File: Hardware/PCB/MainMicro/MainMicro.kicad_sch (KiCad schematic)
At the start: 56 parts, among them J1 Conn_02x05_Odd_Even, J10 Conn_01x03_Male, J11 Conn_01x05_Male, J12 Conn_01x05_Male, J2 USB_B_Mini, J3 Barrel_Jack, J4 Conn_01x05_Male, J5 Conn_01x06_Male, J6 Conn_01x06_Male, J7 Conn_01x03_Male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

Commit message: PCB passing DRC
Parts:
- added R16, R17, R18, R19, R20, R21: 10, Resistor_SMD:R_0805_2012Metric_Pad1.20x1.40mm_HandSolder, symbol Device:R
- J2: footprint Connector_USB:USB_Micro-AB_Molex_47590-0001 -> Connector_USB:USB_Micro-B_Amphenol_10118194_Horizontal
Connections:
- net DIR1+: now also R17.2; no longer U5.20 (B2)
- net DIR2+: now also R20.2; no longer U5.17 (B5)
- net EN1+: now also R18.2; no longer U5.19 (B3)
- net EN2+: now also R21.2; no longer U5.16 (B6)
- net PUL1+: now also R16.2; no longer U5.21 (B1)
- net PUL2+: now also R19.2; no longer U5.18 (B4)
- new net: R21.1, U5.16 (B6)
- new net: R19.1, U5.18 (B4)
- new net: R17.1, U5.20 (B2)
- new net: R16.1, U5.21 (B1)
- new net: R20.1, U5.17 (B5)
- new net: R18.1, U5.19 (B3)
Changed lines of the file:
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@@
     (stroke (width 0) (type default) (color 0 0 0 0))
   )
-  (wire (pts (xy 350.52 128.27) (xy 381 128.27))
+  (wire (pts (xy 350.52 128.27) (xy 360.68 128.27))
     (stroke (width 0) (type default) (color 0 0 0 0))
   )
@@
     (stroke (width 0) (type default) (color 0 0 0 0))
   )
+  (wire (pts (xy 368.3 135.89) (xy 381 135.89))
+    (stroke (width 0) (type default) (color 0 0 0 0))
+  )
   (wire (pts (xy 179.07 88.9) (xy 179.07 93.98))
     (stroke (width 0) (type default) (color 0 0 0 0))
@@
     (stroke (width 0) (type default) (color 0 0 0 0))
   )
+  (wire (pts (xy 368.3 118.11) (xy 381 118.11))
+    (stroke (width 0) (type default) (color 0 0 0 0))
+  )
   (wire (pts (xy 181.61 190.5) (xy 179.07 190.5))
     (stroke (width 0) (type default) (color 0 0 0 0))
@@
     (stroke (width 0) (type default) (color 0 0 0 0))
   )
-  (wire (pts (xy 355.6 118.11) (xy 381 118.11))
+  (wire (pts (xy 355.6 118.11) (xy 360.68 118.11))
     (stroke (width 0) (type default) (color 0 0 0 0))
   )
@@
     (stroke (width 0) (type default) (color 0 0 0 0))
   )
+  (wire (pts (xy 368.3 140.97) (xy 381 140.97))
+    (stroke (width 0) (type default) (color 0 0 0 0))
+  )
   (wire (pts (xy 356.87 198.12) (xy 363.22 198.12))
     (stroke (width 0) (type default) (color 0 0 0 0))
@@
     (stroke (width 0) (type default) (color 0 0 0 0))
   )
+  (wire (pts (xy 368.3 128.27) (xy 381 128.27))
+    (stroke (width 0) (type default) (color 0 0 0 0))
+  )
   (wire (pts (xy 34.29 217.17) (xy 49.53 217.17))
     (stroke (width 0) (type default) (color 0 0 0 0))
@@
     (stroke (width 0) (type default) (color 0 0 0 0))
   )
-  (wire (pts (xy 358.14 135.89) (xy 381 135.89))
+  (wire (pts (xy 358.14 135.89) (xy 360.68 135.89))
     (stroke (width 0) (type default) (color 0 0 0 0))
   )
@@
     (stroke (width 0) (type default) (color 0 0 0 0))
   )
-  (wire (pts (xy 358.14 123.19) (xy 381 123.19))
+  (wire (pts (xy 358.14 123.19) (xy 360.68 123.19))
     (stroke (width 0) (type default) (color 0 0 0 0))
   )
@@
     (stroke (width 0) (type default) (color 0 0 0 0))
   )
-  (wire (pts (xy 353.06 146.05) (xy 381 146.05))
+  (wire (pts (xy 353.06 146.05) (xy 360.68 146.05))
     (stroke (width 0) (type default) (color 0 0 0 0))
   )
@@
     (stroke (width 0) (type default) (color 0 0 0 0))
   )
+  (wire (pts (xy 368.3 146.05) (xy 381 146.05))
+    (stroke (width 0) (type default) (color 0 0 0 0))
+  )
   (wire (pts (xy 336.55 167.64) (xy 344.17 167.64))
     (stroke (width 0) (type default) (color 0 0 0 0))
@@
     (stroke (width 0) (type default) (color 0 0 0 0))
   )
-  (wire (pts (xy 355.6 140.97) (xy 381 140.97))
+  (wire (pts (xy 355.6 140.97) (xy 360.68 140.97))
     (stroke (width 0) (type default) (color 0 0 0 0))
   )
@@
     (stroke (width 0) (type default) (color 0 0 0 0))
   )
+  (wire (pts (xy 368.3 123.19) (xy 381 123.19))
+    (stroke (width 0) (type default) (color 0 0 0 0))
+  )
   (polyline (pts (xy 12.7 205.74) (xy 66.04 205.74))
     (stroke (width 0) (type default) (color 0 0 0 0))
@@
   (symbol (lib_id "power:PWR_FLAG") (at 33.02 62.23 270) (unit 1)
     (in_bom yes) (on_board yes)
-    (property "Reference" "#FLG?" (id 0) (at 34.925 62.23 0)
+    (property "Reference" "#FLG03" (id 0) (at 34.925 62.23 0)
       (effects (font (size 1.27 1.27)) hide)
     )
@@
     (pin "1")
   )
+  (symbol (lib_id "Device:R") (at 364.49 146.05 90) (unit 1)
+    (in_bom yes) (on_board yes)
+    (property "Reference" "R21" (id 0) (at 368.3 144.78 90))
+    (property "Value" "10" (id 1) (at 364.49 146.05 90))
+    (property "Footprint" "Resistor_SMD:R_0805_2012Metric_Pad1.20x1.40mm_HandSolder" (id 2) (at 364.49 147.828 90)
+      (effects (font (size 1.27 1.27)) hide)
+    )
+    (property "Datasheet" "~" (id 3) (at 364.49 146.05 0)
+      (effects (font (size 1.27 1.27)) hide)
+    )
+    (pin "1")
+    (pin "2")
+  )
   (symbol (lib_id "Device:Ferrite_Bead_Small") (at 133.35 31.75 270) (unit 1)
     (in_bom yes) (on_board yes)
@@
     (pin "1")
   )
+  (symbol (lib_id "Device:R") (at 364.49 135.89 90) (unit 1)
+    (in_bom yes) (on_board yes)
+    (property "Reference" "R19" (id 0) (at 368.3 134.62 90))
+    (property "Value" "10" (id 1) (at 364.49 135.89 90))
+    (property "Footprint" "Resistor_SMD:R_0805_2012Metric_Pad1.20x1.40mm_HandSolder" (id 2) (at 364.49 137.668 90)
+      (effects (font (size 1.27 1.27)) hide)
+    )
+    (property "Datasheet" "~" (id 3) (at 364.49 135.89 0)
+      (effects (font (size 1.27 1.27)) hide)
+    )
+    (pin "1")
+    (pin "2")
+  )
   (symbol (lib_id "Device:C") (at 346.71 109.22 270) (unit 1)
     (in_bom yes) (on_board yes)
@@
     (pin "2")
   )
+  (symbol (lib_id "Device:R") (at 364.49 123.19 90) (unit 1)
+    (in_bom yes) (on_board yes)
+    (property "Reference" "R17" (id 0) (at 368.3 121.92 90))
+    (property "Value" "10" (id 1) (at 364.49 123.19 90))
+    (property "Footprint" "Resistor_SMD:R_0805_2012Metric_Pad1.20x1.40mm_HandSolder" (id 2) (at 364.49 124.968 90)
+      (effects (font (size 1.27 1.27)) hide)
+    )
+    (property "Datasheet" "~" (id 3) (at 364.49 123.19 0)
+      (effects (font (size 1.27 1.27)) hide)
+    )
+    (pin "1")
+    (pin "2")
+  )
   (symbol (lib_id "power:GND") (at 353.06 26.67 90) (unit 1)
     (in_bom yes) (on_board yes) (fields_autoplaced)
@@
     (pin "1")
   )
+  (symbol (lib_id "Device:R") (at 364.49 118.11 90) (unit 1)
+    (in_bom yes) (on_board yes)
+    (property "Reference" "R16" (id 0) (at 368.3 116.84 90))
+    (property "Value" "10" (id 1) (at 364.49 118.11 90))
+    (property "Footprint" "Resistor_SMD:R_0805_2012Metric_Pad1.20x1.40mm_HandSolder" (id 2) (at 364.49 119.888 90)
+      (effects (font (size 1.27 1.27)) hide)
+    )
+    (property "Datasheet" "~" (id 3) (at 364.49 118.11 0)
+      (effects (font (size 1.27 1.27)) hide)
+    )
+    (pin "1")
+    (pin "2")
+  )
   (symbol (lib_id "power:GND") (at 358.14 182.88 270) (unit 1)
     (in_bom yes) (on_board yes) (fields_autoplaced)
@@
       (effects (font (size 1.27 1.27)) (justify right))
     )
-    (property "Footprint" "Connector_USB:USB_Micro-AB_Molex_47590-0001" (id 2) (at 382.27 44.45 0)
+    (property "Footprint" "Connector_USB:USB_Micro-B_Amphenol_10118194_Horizontal" (id 2) (at 382.27 44.45 0)
       (effects (font (size 1.27 1.27)) hide)
     )
@@
     (pin "2")
   )
+  (symbol (lib_id "Device:R") (at 364.49 140.97 90) (unit 1)
+    (in_bom yes) (on_board yes)
+    (property "Reference" "R20" (id 0) (at 368.3 139.7 90))
+    (property "Value" "10" (id 1) (at 364.49 140.97 90))
+    (property "Footprint" "Resistor_SMD:R_0805_2012Metric_Pad1.20x1.40mm_HandSolder" (id 2) (at 364.49 142.748 90)
+      (effects (font (size 1.27 1.27)) hide)
+    )
+    (property "Datasheet" "~" (id 3) (at 364.49 140.97 0)
+      (effects (font (size 1.27 1.27)) hide)
+    )
+    (pin "1")
+    (pin "2")
+  )
   (symbol (lib_id "Mechanical:MountingHole") (at 20.32 278.13 0) (unit 1)
     (in_bom yes) (on_board yes) (fields_autoplaced)
@@
     (pin "2")
   )
+  (symbol (lib_id "Device:R") (at 364.49 128.27 90) (unit 1)
+    (in_bom yes) (on_board yes)
+    (property "Reference" "R18" (id 0) (at 368.3 127 90))
+    (property "Value" "10" (id 1) (at 364.49 128.27 90))
+    (property "Footprint" "Resistor_SMD:R_0805_2012Metric_Pad1.20x1.40mm_HandSolder" (id 2) (at 364.49 130.048 90)
+      (effects (font (size 1.27 1.27)) hide)
+    )
+    (property "Datasheet" "~" (id 3) (at 364.49 128.27 0)
+      (effects (font (size 1.27 1.27)) hide)
+    )
+    (pin "1")
+    (pin "2")
+  )
   (symbol (lib_id "power:+3.3V") (at 48.26 25.4 0) (unit 1)
     (in_bom yes) (on_board yes) (fields_autoplaced)
@@
     )
     (path "/06481be9-17d5-4348-8cf3-2ac380ada025"
-      (reference "#FLG?") (unit 1) (value "PWR_FLAG") (footprint "")
+      (reference "#FLG03") (unit 1) (value "PWR_FLAG") (footprint "")
     )
     (path "/509860c8-fe7c-4cfb-b131-6975ab45b37f"
@@
     )
     (path "/873c612d-f5e5-451f-9631-74bf26e685d0"
-      (reference "J2") (unit 1) (value "USB_B_Mini") (footprint "Connector_USB:USB_Micro-AB_Molex_47590-0001")
+      (reference "J2") (unit 1) (value "USB_B_Mini") (footprint "Connector_USB:USB_Micro-B_Amphenol_10118194_Horizontal")
     )
     (path "/89c18b9c-1cb9-45ef-bf7e-879d882b206b"
@@
       (reference "R15") (unit 1) (value "10") (footprint "Resistor_SMD:R_0805_2012Metric_Pad1.20x1.40mm_HandSolder")
     )
+    (path "/6141450e-8891-4e46-a481-d7396799fbbe"
+      (reference "R16") (unit 1) (value "10") (footprint "Resistor_SMD:R_0805_2012Metric_Pad1.20x1.40mm_HandSolder")
+    )
+    (path "/420fe823-ea59-4aca-8e65-c1fec0abf738"
+      (reference "R17") (unit 1) (value "10") (footprint "Resistor_SMD:R_0805_2012Metric_Pad1.20x1.40mm_HandSolder")
+    )
+    (path "/e22916f6-ce35-496d-b7b1-1208e8e8071e"
+      (reference "R18") (unit 1) (value "10") (footprint "Resistor_SMD:R_0805_2012Metric_Pad1.20x1.40mm_HandSolder")
+    )
+    (path "/35dfe0d1-7c61-4f1c-8456-3f0475c0a93a"
+      (reference "R19") (unit 1) (value "10") (footprint "Resistor_SMD:R_0805_2012Metric_Pad1.20x1.40mm_HandSolder")
+    )
+    (path "/bf6bb947-f5bc-49a9-8660-df01cd5a6510"
+      (reference "R20") (unit 1) (value "10") (footprint "Resistor_SMD:R_0805_2012Metric_Pad1.20x1.40mm_HandSolder")
+    )
+    (path "/2db6640c-74f0-4ddd-84d1-00c533095472"
+      (reference "R21") (unit 1) (value "10") (footprint "Resistor_SMD:R_0805_2012Metric_Pad1.20x1.40mm_HandSolder")
+    )
     (path "/4e21c3da-75a8-4c76-ab94-27497c4c11e3"

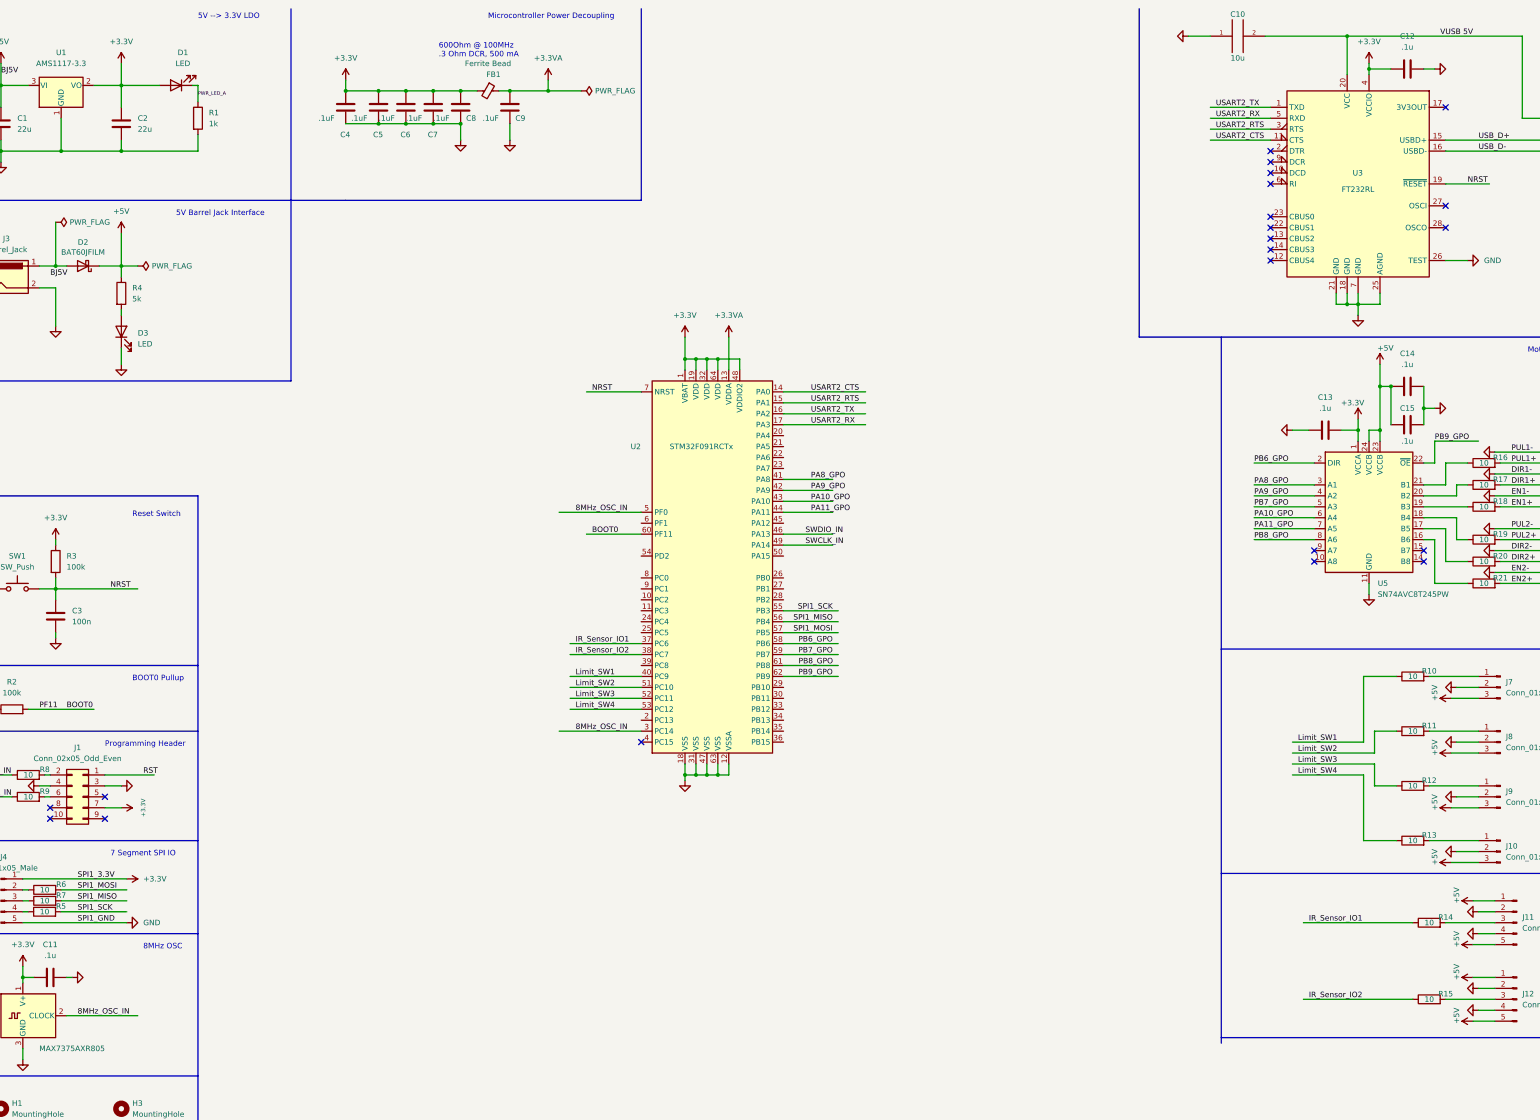
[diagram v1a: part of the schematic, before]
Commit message: Fixed Joe concerns
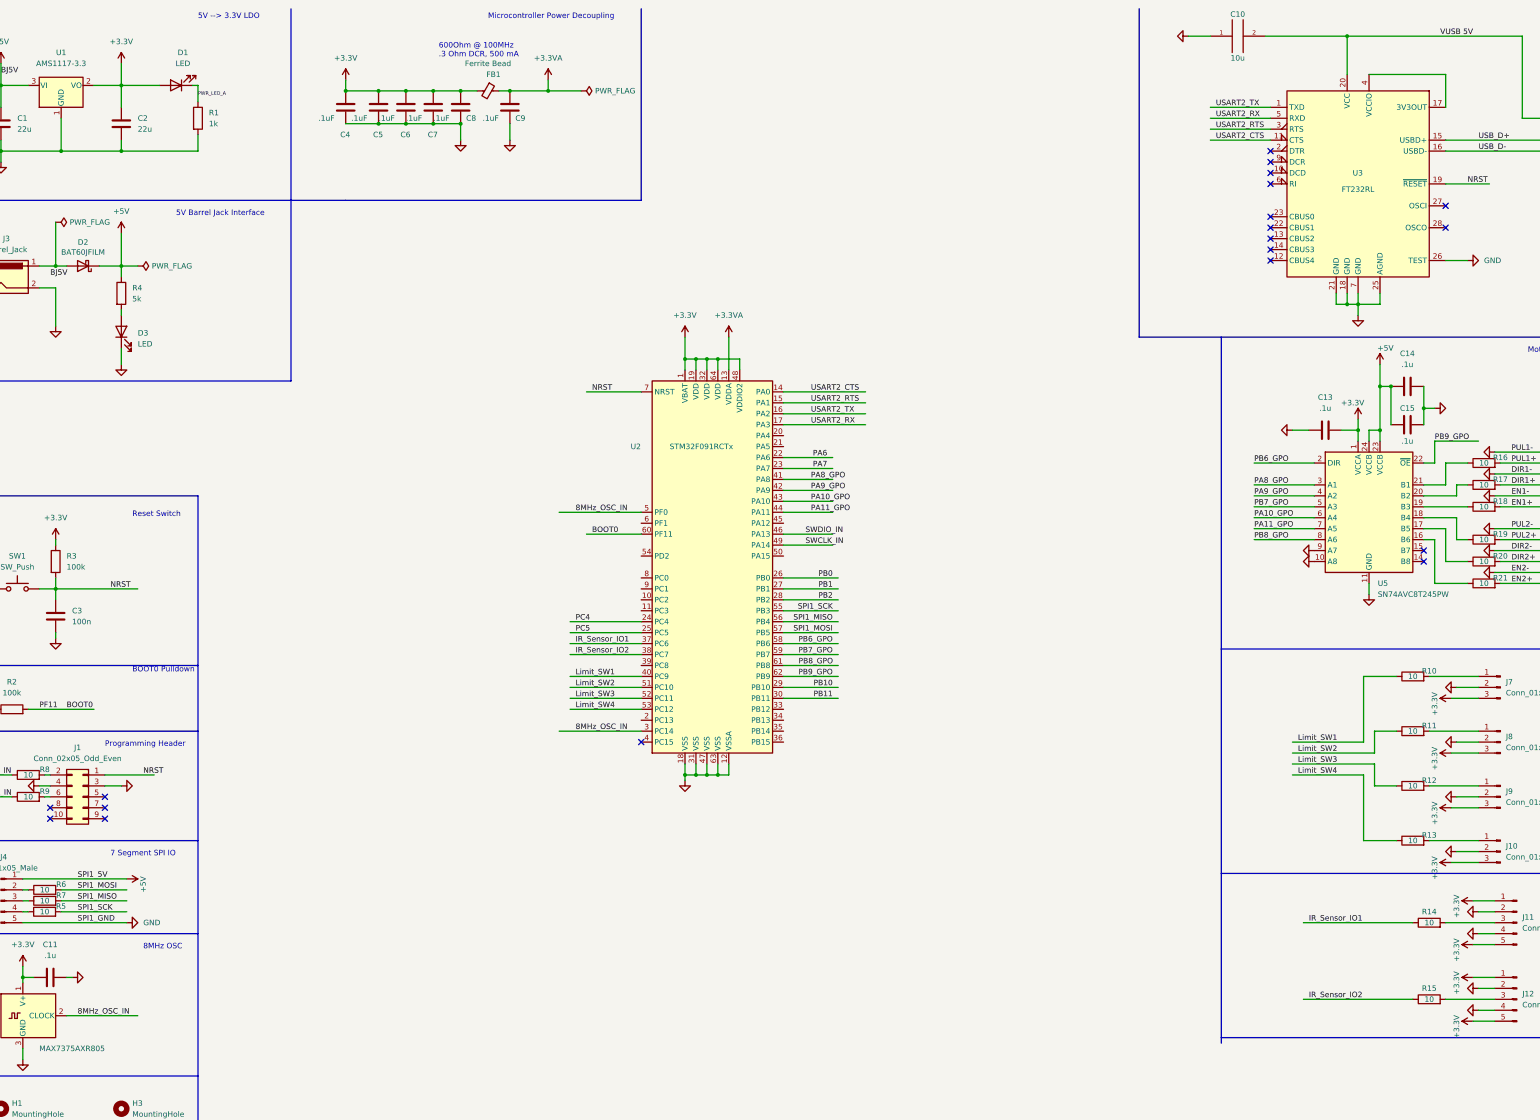
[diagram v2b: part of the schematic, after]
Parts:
- removed C12: .1u, Capacitor_SMD:C_0805_2012Metric_Pad1.18x1.45mm_HandSolder, symbol Device:C
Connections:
- net RST is gone; now on net NRST: J1.1 (Pin_1)
- net +3V3: now also J10.3 (Pin_3), J11.1 (Pin_1), J11.5 (Pin_5), J12.1 (Pin_1), J12.5 (Pin_5), J7.3 (Pin_3), J8.3 (Pin_3), J9.3 (Pin_3); no longer J1.7 (Pin_7), J4.1 (Pin_1), U3.4 (VCCIO)
- net +5V: now also J4.1 (Pin_1); no longer J10.3 (Pin_3), J11.1 (Pin_1), J11.5 (Pin_5), J12.1 (Pin_1), J12.5 (Pin_5), J7.3 (Pin_3), J8.3 (Pin_3), J9.3 (Pin_3)
- net GND: now also U5.10 (A8), U5.9 (A7)
- net PA6: now reaches U2.22 (PA6)
- net PA7: now reaches U2.23 (PA7)
- net PC4: now reaches U2.24 (PC4)
- net PC5: now reaches U2.25 (PC5)
- net PB0: now reaches U2.26 (PB0)
- net PB1: now reaches U2.27 (PB1)
- net PB2: now reaches U2.28 (PB2)
- net PB10: now reaches U2.29 (PB10)
- net PB11: now reaches U2.30 (PB11)
- net at U3.17 (3V3OUT): now also U3.4 (VCCIO)
- no-connect marks 23 -> 21
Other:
- note added: "BOOT0 Pulldown"
- note removed: "BOOT0 Pullup"
